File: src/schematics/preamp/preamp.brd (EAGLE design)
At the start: 50.8 x 35.6 mm, 33 parts

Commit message: Added input protection resistor to preamp
Ah input resistor was added to preamp inputs, so that short circuits of
clamping diodes won't hurt the connected device outputs.

Andrea Zoppi
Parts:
- added R17, R18: 1k, rcl:0204/5
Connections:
- new net N$3: C3.-, D3.A, D4.C, R18.2, R2.2
- new net N$8: C2.-, D1.A, D2.C, R17.2, R4.2
- net INA: now also R17.1; no longer C2.-, D1.A, D2.C, R4.2
- net INB: now also R18.1; no longer C3.-, D3.A, D4.C, R2.2
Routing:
- net N$3: track 0.00 -> 7.96 mm
- net INB: track 7.96 -> 0.00 mm
- net N$8: track 0.00 -> 7.96 mm
- net INA: track 7.96 -> 0.00 mm
- net VA: track 37.3 -> 36.2 mm
- net VB: track 36.9 -> 36.2 mm
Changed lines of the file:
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@@
 <text x="50.8" y="33.655" size="1.778" layer="51" rot="R90">G</text>
 <text x="50.8" y="31.75" size="1.778" layer="51" rot="R90">P</text>
-<text x="11.43" y="13.97" size="1.778" layer="48" rot="R90">TODO</text>
+<text x="12.7" y="10.16" size="1.778" layer="48" rot="R90">TODO</text>
 </plain>
 <attributes>
@@
 </element>
 <element name="D1" library="diode_local" package="DO35-5" value="1N4148" x="34.925" y="35.2425" smashed="yes" rot="R270">
-<attribute name="NAME" x="33.3375" y="28.829" size="1.27" layer="25" ratio="10" rot="R90"/>
+<attribute name="NAME" x="33.3375" y="27.559" size="1.27" layer="25" ratio="10" rot="R90"/>
 </element>
 <element name="D2" library="diode_local" package="DO35-5" value="1N4148" x="37.465" y="36.83" smashed="yes" rot="R90">
-<attribute name="NAME" x="34.925" y="28.829" size="1.27" layer="25" ratio="10" rot="R90"/>
+<attribute name="NAME" x="34.925" y="27.559" size="1.27" layer="25" ratio="10" rot="R90"/>
 </element>
 <element name="D3" library="diode_local" package="DO35-5" value="1N4148" x="34.925" y="10.4775" smashed="yes" rot="R90">
-<attribute name="NAME" x="33.655" y="14.5415" size="1.27" layer="25" ratio="10" rot="R90"/>
+<attribute name="NAME" x="33.655" y="16.129" size="1.27" layer="25" ratio="10" rot="R90"/>
 </element>
 <element name="D4" library="diode_local" package="DO35-5" value="1N4148" x="37.465" y="8.89" smashed="yes" rot="R270">
-<attribute name="NAME" x="35.2425" y="14.5415" size="1.27" layer="25" ratio="10" rot="R90"/>
+<attribute name="NAME" x="35.2425" y="16.129" size="1.27" layer="25" ratio="10" rot="R90"/>
 </element>
 <element name="D5" library="diode_local" package="DO35-5" value="1N4148" x="11.43" y="33.02" smashed="yes" rot="R270">
@@
 <element name="C1" library="rcl" package="E2-4" value="1u5" x="48.26" y="7.62" smashed="yes" rot="R270">
 <attribute name="NAME" x="49.149" y="9.779" size="1.27" layer="25" ratio="10"/>
+</element>
+<element name="R17" library="rcl" package="0204/5" value="1k" x="12.7" y="22.86" smashed="yes">
+<attribute name="NAME" x="11.3284" y="22.4409" size="0.9906" layer="25" ratio="10"/>
+</element>
+<element name="R18" library="rcl" package="0204/5" value="1k" x="12.7" y="20.32" smashed="yes">
+<attribute name="NAME" x="11.3284" y="19.9009" size="0.9906" layer="25" ratio="10"/>
 </element>
 </elements>
@@
 </signal>
 <signal name="INA">
-<contactref element="R4" pad="2"/>
-<contactref element="D1" pad="A"/>
-<contactref element="D2" pad="C"/>
-<contactref element="C2" pad="-"/>
-<wire x1="39.6875" y1="31.75" x2="39.6875" y2="34.29" width="0.6096" layer="16"/>
-<wire x1="39.6875" y1="34.29" x2="37.465" y2="34.29" width="0.6096" layer="16"/>
-<wire x1="34.925" y1="32.7025" x2="35.8775" y2="32.7025" width="0.6096" layer="16"/>
-<wire x1="35.8775" y1="32.7025" x2="37.465" y2="34.29" width="0.6096" layer="16"/>
+<contactref element="R17" pad="1"/>
 </signal>
 <signal name="BIAS">
@@
 <contactref element="U1" pad="3"/>
 <contactref element="U1" pad="12"/>
-<wire x1="22.225" y1="16.51" x2="22.225" y2="20.32" width="0.6096" layer="16"/>
-<wire x1="22.225" y1="20.32" x2="23.495" y2="21.59" width="0.6096" layer="16"/>
-<wire x1="23.495" y1="21.59" x2="33.02" y2="21.59" width="0.6096" layer="16"/>
+<wire x1="22.225" y1="16.51" x2="22.225" y2="20.6375" width="0.6096" layer="16"/>
+<wire x1="22.225" y1="20.6375" x2="23.1775" y2="21.59" width="0.6096" layer="16"/>
+<wire x1="23.1775" y1="21.59" x2="33.02" y2="21.59" width="0.6096" layer="16"/>
 <wire x1="33.02" y1="21.59" x2="34.29" y2="20.32" width="0.6096" layer="16"/>
 <wire x1="34.29" y1="20.32" x2="34.29" y2="19.05" width="0.6096" layer="16"/>
@@
 </signal>
 <signal name="INB">
-<contactref element="R2" pad="2"/>
-<contactref element="D3" pad="A"/>
-<contactref element="D4" pad="C"/>
-<contactref element="C3" pad="-"/>
-<wire x1="39.6875" y1="13.97" x2="39.6875" y2="11.43" width="0.6096" layer="16"/>
-<wire x1="39.6875" y1="11.43" x2="37.465" y2="11.43" width="0.6096" layer="16"/>
-<wire x1="34.925" y1="13.0175" x2="35.8775" y2="13.0175" width="0.6096" layer="16"/>
-<wire x1="35.8775" y1="13.0175" x2="37.465" y2="11.43" width="0.6096" layer="16"/>
+<contactref element="R18" pad="1"/>
 </signal>
 <signal name="N$9">
@@
 <wire x1="39.37" y1="26.67" x2="39.37" y2="25.4" width="0.6096" layer="16"/>
 <wire x1="39.37" y1="25.4" x2="38.1" y2="24.13" width="0.6096" layer="16"/>
-<wire x1="38.1" y1="24.13" x2="36.83" y2="24.13" width="0.6096" layer="16"/>
-<via x="36.83" y="24.13" extent="1-16" drill="0.6" shape="square"/>
-<wire x1="36.83" y1="24.13" x2="21.59" y2="24.13" width="0.6096" layer="1"/>
-<via x="21.59" y="24.13" extent="1-16" drill="0.6" diameter="1.27" shape="octagon"/>
-<wire x1="21.59" y1="24.13" x2="21.59" y2="26.035" width="0.6096" layer="16"/>
+<via x="38.1" y="24.13" extent="1-16" drill="0.6" diameter="1.27" shape="octagon"/>
+<wire x1="38.1" y1="24.13" x2="23.495" y2="24.13" width="0.6096" layer="1"/>
+<wire x1="23.495" y1="24.13" x2="21.59" y2="26.035" width="0.6096" layer="1"/>
+<via x="21.59" y="26.035" extent="1-16" drill="0.6" diameter="1.27" shape="octagon"/>
 <wire x1="21.59" y1="26.035" x2="18.415" y2="29.21" width="0.6096" layer="16"/>
 <wire x1="18.415" y1="29.21" x2="17.78" y2="29.21" width="0.6096" layer="16"/>
@@
 <wire x1="39.37" y1="19.05" x2="39.37" y2="20.32" width="0.6096" layer="16"/>
 <wire x1="39.37" y1="20.32" x2="38.1" y2="21.59" width="0.6096" layer="16"/>
-<wire x1="38.1" y1="21.59" x2="36.83" y2="21.59" width="0.6096" layer="16"/>
-<via x="36.83" y="21.59" extent="1-16" drill="0.6" diameter="1.27" shape="octagon"/>
-<wire x1="36.83" y1="21.59" x2="21.59" y2="21.59" width="0.6096" layer="1"/>
-<wire x1="21.59" y1="21.59" x2="19.05" y2="24.13" width="0.6096" layer="1"/>
-<via x="19.05" y="24.13" extent="1-16" drill="0.6" diameter="1.27" shape="octagon"/>
-<wire x1="19.05" y1="24.13" x2="19.05" y2="25.4" width="0.6096" layer="16"/>
-<wire x1="19.05" y1="25.4" x2="17.78" y2="26.67" width="0.6096" layer="16"/>
+<via x="38.1" y="21.59" extent="1-16" drill="0.6" diameter="1.27" shape="octagon"/>
+<wire x1="38.1" y1="21.59" x2="22.86" y2="21.59" width="0.6096" layer="1"/>
+<wire x1="22.86" y1="21.59" x2="20.32" y2="24.13" width="0.6096" layer="1"/>
+<via x="20.32" y="24.13" extent="1-16" drill="0.6" diameter="1.27" shape="octagon"/>
+<wire x1="20.32" y1="24.13" x2="17.78" y2="26.67" width="0.6096" layer="16"/>
 </signal>
 <signal name="N$6">
@@
 <contactref element="R14" pad="1"/>
 <contactref element="U1" pad="7"/>
-<wire x1="24.13" y1="26.67" x2="24.13" y2="24.13" width="0.6096" layer="16"/>
-<wire x1="24.13" y1="24.13" x2="19.685" y2="19.685" width="0.6096" layer="16"/>
-<wire x1="19.685" y1="19.685" x2="19.685" y2="17.78" width="0.6096" layer="16"/>
+<wire x1="24.13" y1="26.67" x2="24.13" y2="24.765" width="0.6096" layer="16"/>
+<wire x1="24.13" y1="24.765" x2="19.685" y2="20.32" width="0.6096" layer="16"/>
+<wire x1="19.685" y1="20.32" x2="19.685" y2="17.78" width="0.6096" layer="16"/>
+</signal>
+<signal name="N$2">
+</signal>
+<signal name="N$3">
+<contactref element="R18" pad="2"/>
+<contactref element="C3" pad="-"/>
+<contactref element="D3" pad="A"/>
+<contactref element="D4" pad="C"/>
+<contactref element="R2" pad="2"/>
+<wire x1="39.6875" y1="13.97" x2="39.6875" y2="11.43" width="0.6096" layer="16"/>
+<wire x1="39.6875" y1="11.43" x2="37.465" y2="11.43" width="0.6096" layer="16"/>
+<wire x1="37.465" y1="11.43" x2="36.5125" y2="11.43" width="0.6096" layer="16"/>
+<wire x1="36.5125" y1="11.43" x2="34.925" y2="13.0175" width="0.6096" layer="16"/>
+<wire x1="15.24" y1="20.32" x2="34.925" y2="13.0175" width="0" layer="19" extent="1-1"/>
+</signal>
+<signal name="N$8">
+<contactref element="R17" pad="2"/>
+<contactref element="C2" pad="-"/>
+<contactref element="D1" pad="A"/>
+<contactref element="D2" pad="C"/>
+<contactref element="R4" pad="2"/>
+<wire x1="39.6875" y1="31.75" x2="39.6875" y2="34.29" width="0.6096" layer="16"/>
+<wire x1="39.6875" y1="34.29" x2="37.465" y2="34.29" width="0.6096" layer="16"/>
+<wire x1="37.465" y1="34.29" x2="36.5125" y2="34.29" width="0.6096" layer="16"/>
+<wire x1="36.5125" y1="34.29" x2="34.925" y2="32.7025" width="0.6096" layer="16"/>
+<wire x1="15.24" y1="22.86" x2="34.925" y2="32.7025" width="0" layer="19" extent="1-1"/>
 </signal>
 </signals>

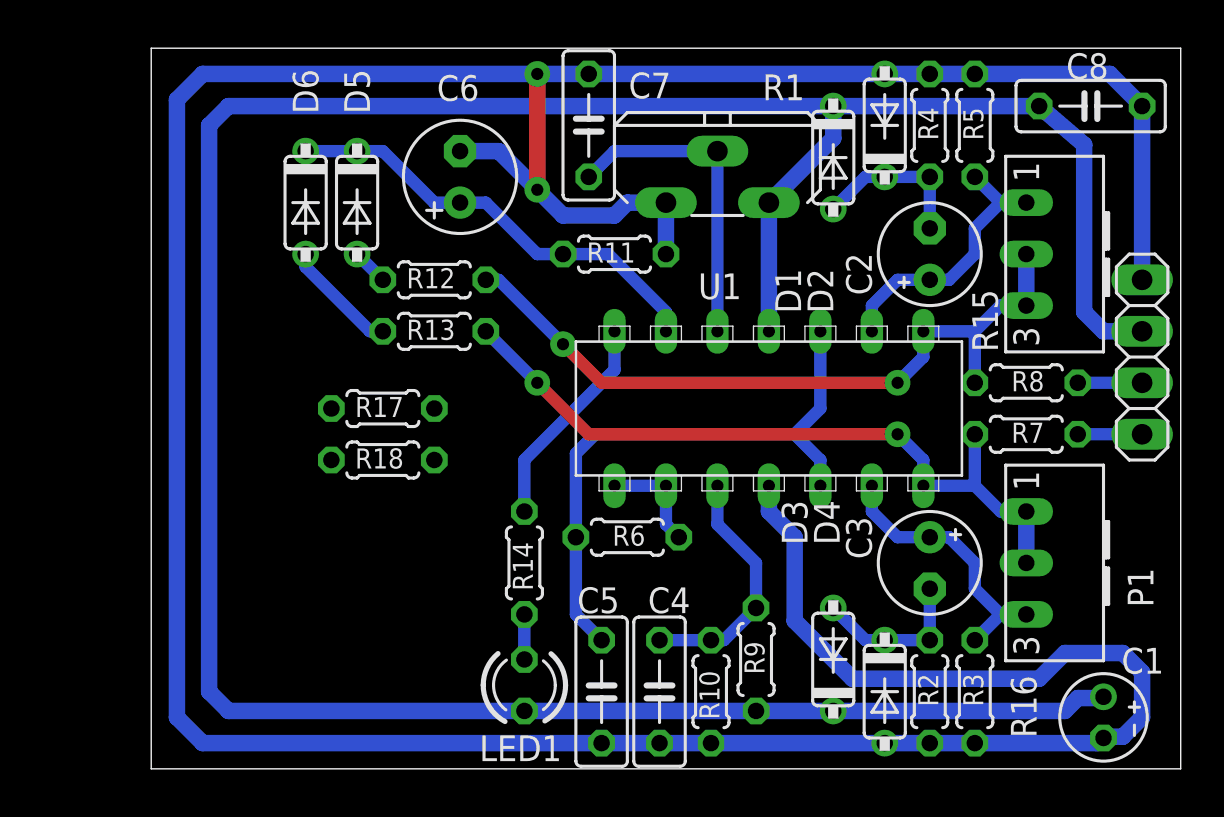
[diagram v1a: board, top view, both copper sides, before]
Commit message: Added double RCA connector to preamp module
Andrea Zoppi
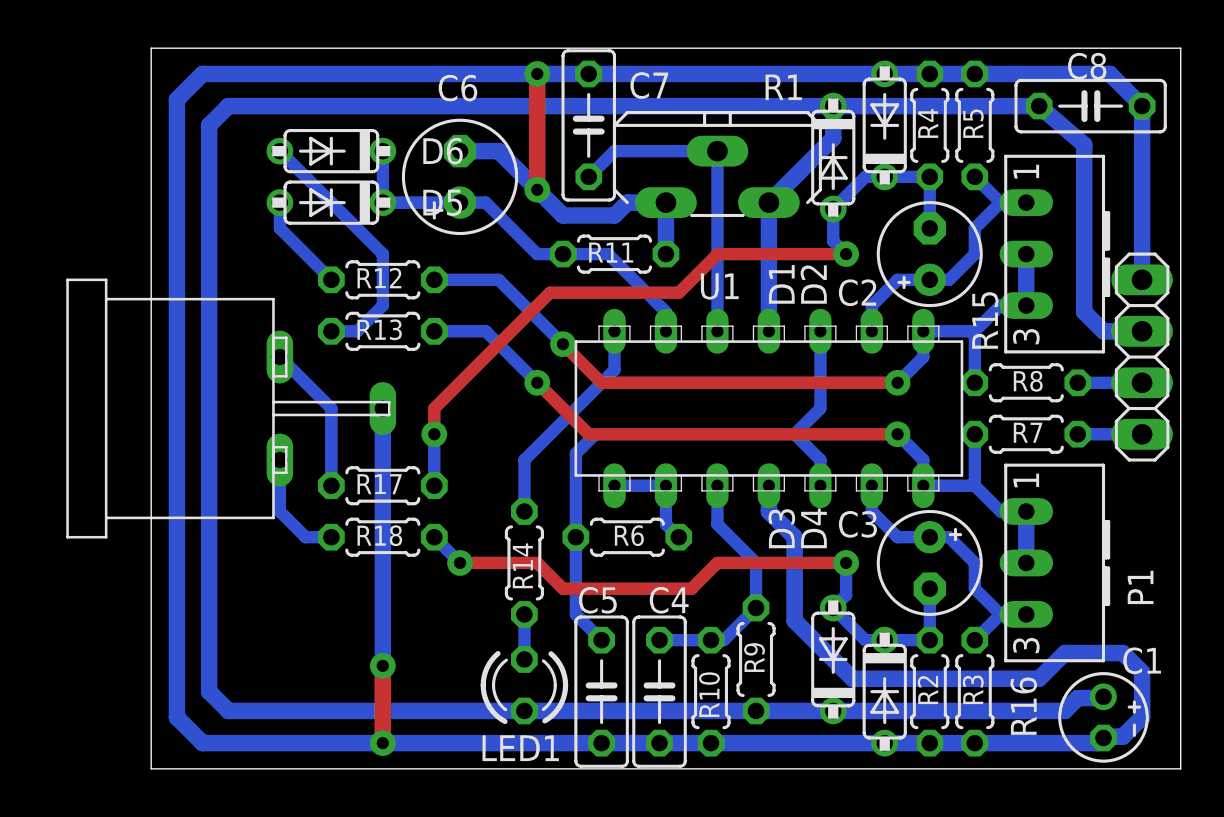
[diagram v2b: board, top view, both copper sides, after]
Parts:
- added RCA1: RCA-2V, con_local:RCA-2V
- moved R17 3.81 mm to (12.7, 19.1)
- moved R18 3.81 mm to (12.7, 16.5)
- moved D6 2.84 mm to (10.2, 35.6), turned to 180 degrees
- moved R12 2.54 mm to (12.7, 29.2)
- moved R13 2.54 mm to (12.7, 26.7)
- moved D5 1.27 mm to (10.2, 33.0), turned to 180 degrees
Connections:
- net GND: now also RCA1.SHIELD
- net INA: now also RCA1.L
- net INB: now also RCA1.R
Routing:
- net N$8: track 7.96 -> 37.7 mm, vias 0 -> 2
- net N$3: track 7.96 -> 32.3 mm, vias 0 -> 2
- net GND: track 185.2 -> 201.7 mm, vias 2 -> 4
- net INA: track 0.00 -> 7.40 mm
- net N$11: track 5.76 -> 12.8 mm
- net INB: track 0.00 -> 5.61 mm
- net N$10: track 1.80 -> 4.86 mm
- net VB: track 36.2 -> 38.7 mm
- net VA: track 36.2 -> 38.7 mm
- net N$4: track 22.0 -> 19.7 mm
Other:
- board text removed: "TODO"

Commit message: Trimmable preamp positive reference
The preamp positive voltage reference is now trimmable, so that it can be
calibrated in order to reduce misalignments with the main board's internal
reference (internal DAC output of the PIC).

Preamp board schematics refactored.

Andrea Zoppi
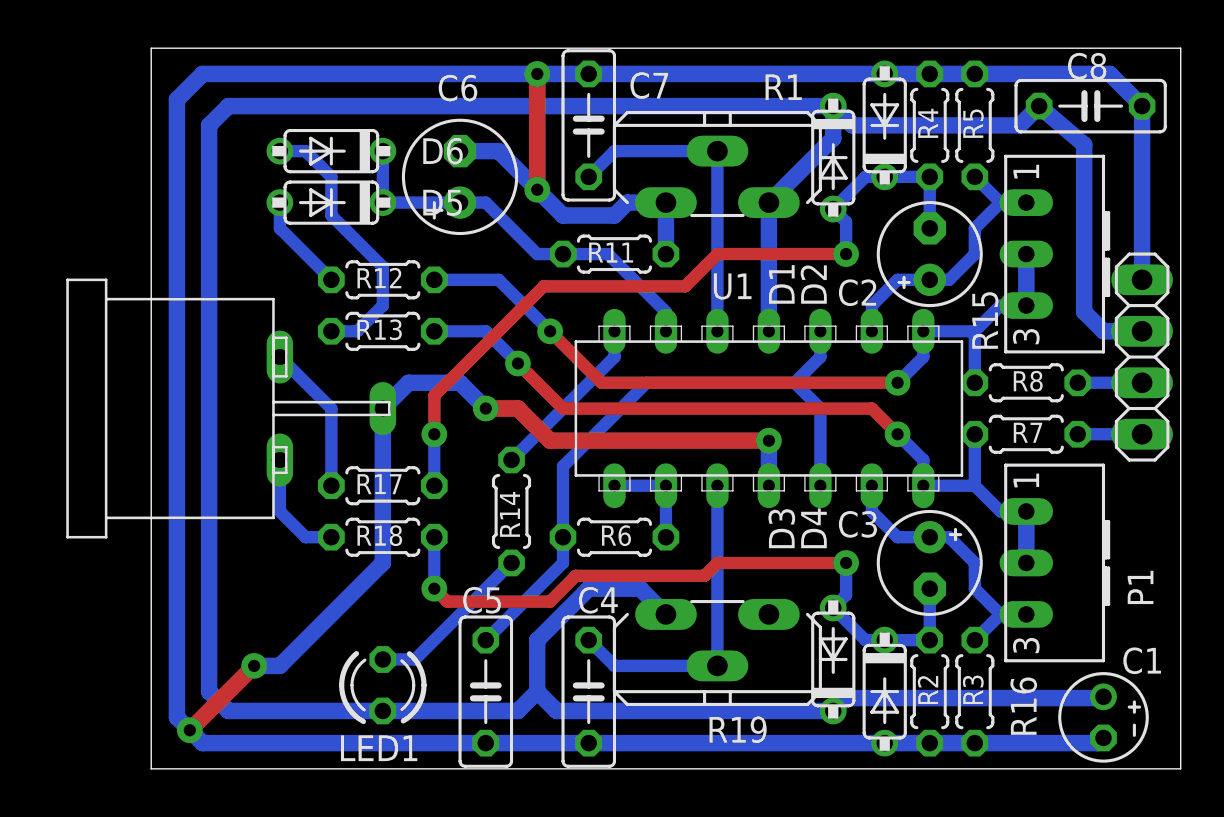
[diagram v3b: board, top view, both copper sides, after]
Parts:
- removed R10, R9: 10k, rcl:0204/5
- added R19: 47k, pot:PT-10S
- moved LED1 6.98 mm to (12.7, 9.21)
- moved C5 5.71 mm to (17.8, 8.89)
- moved C4 3.49 mm to (22.9, 8.89)
- moved R14 2.62 mm to (19.1, 17.8)
- moved R6 0.64 mm to (24.1, 16.5)
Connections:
- new net N$14: R19.A
- net +3V3: now also R19.E; no longer R9.2
- net GND: no longer R10.1
- net N$1: now also R19.S; no longer R10.2, R9.1
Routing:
- net +3V3: track 140.9 -> 153.0 mm
- net N$12: track 2.22 -> 8.32 mm
- net GND: track 201.7 -> 197.8 mm, vias 4 -> 6
- net N$1: track 12.2 -> 15.8 mm
- net BIAS: track 29.6 -> 32.0 mm
- net N$13: track 10.7 -> 8.45 mm
- net N$3: track 32.3 -> 34.4 mm
- net N$11: track 12.8 -> 13.5 mm

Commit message: Window comparator for preamp calibration
The positive voltage reference for opamps is now reduced to a simple
potentiometer, sithout impedance decoupling (not strictly needed).

Two opamps are used as comparators for windowing of the rectified input
signals. This way it is possible to warn the user if the signal is too low
like before (bad comparator results) and also if the signal is too strong,
thus leading to a potentially wring duty cycle of the squared wave.

Andrea Zoppi
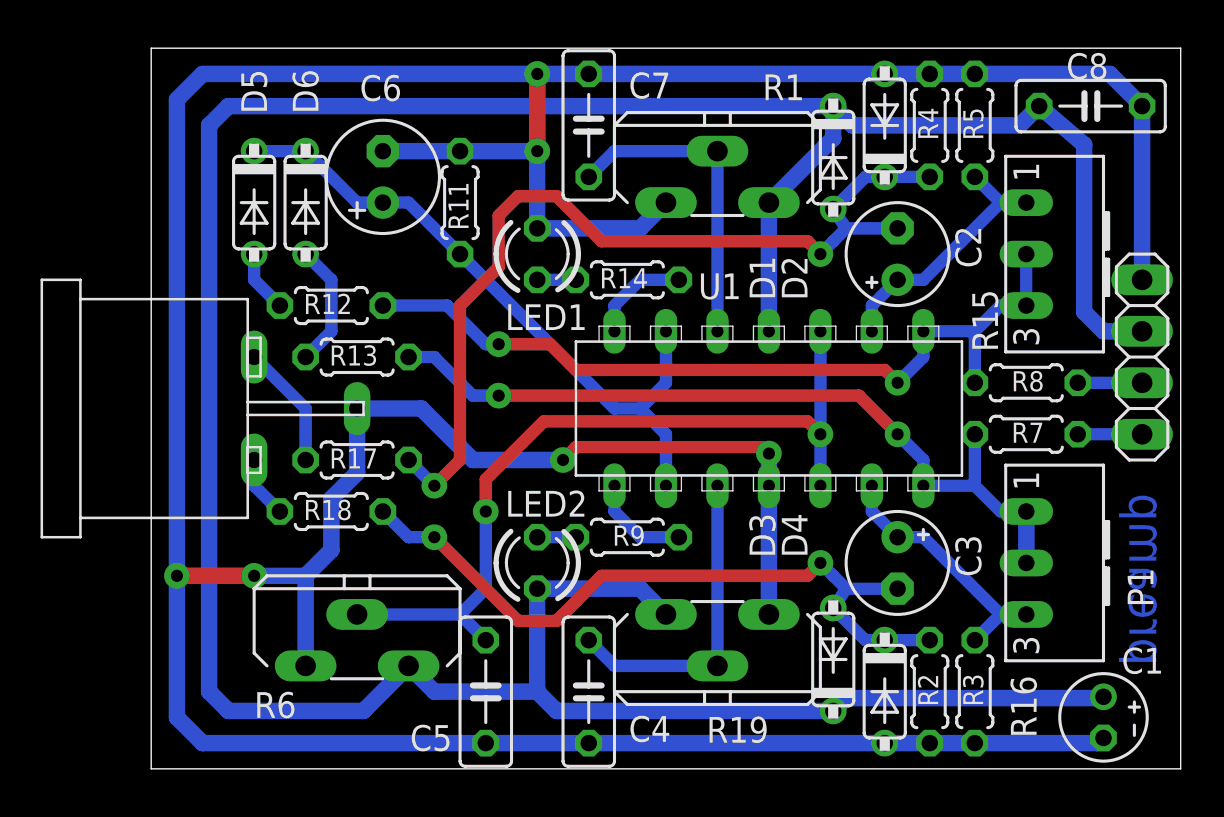
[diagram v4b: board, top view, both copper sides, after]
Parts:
- added LED2: red, led:LED3MM
- added R9: 470, rcl:0204/5
- R6: value 1k -> 47k; device rcl:0204/5 -> pot:PT-10S
- moved LED1 22.6 mm to (20.3, 30.5)
- moved R6 13.7 mm to (11.4, 11.4), turned to 0 degrees
- moved R14 12.8 mm to (24.8, 29.2), turned to 180 degrees
- moved R11 8.03 mm to (16.5, 33.0), turned to 270 degrees
- moved C6 3.81 mm to (12.7, 34.3)
- moved D5 3.81 mm to (6.35, 33.0), turned to 270 degrees
- moved D6 2.84 mm to (8.89, 33.0), turned to 270 degrees
- moved R12 2.84 mm to (10.2, 27.9)
- moved R18 2.84 mm to (10.2, 17.8)
- moved R13 1.80 mm to (11.4, 25.4)
- moved R17 1.80 mm to (11.4, 20.3)
- moved C2 1.59 mm to (38.1, 30.5)
- moved C3 1.59 mm to (38.1, 15.2)
- moved RCA1 1.27 mm to (8.89, 22.9)
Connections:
- net INA renamed INL
- net INB renamed INR
- net OUTA renamed OUTL
- net OUTB renamed OUTR
- net VA renamed VL
- net VB renamed VR
- removed net N$14: R19.A
- new net N$2: R9.1, U1.8
- net +3V3: now also LED2.A, R6.E; no longer LED1.A
- net BIAS: now also R6.S; no longer R6.2
- net GND: now also LED1.K, R19.A, R6.A
- net N$12: now also LED2.K, R9.2; no longer LED1.K, R14.2
- net N$4: now also U1.9
- net N$7: now also LED1.A, R14.2; no longer R6.1, U1.8, U1.9
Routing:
- net N$4: track 19.7 -> 33.0 mm
- net GND: track 197.8 -> 206.2 mm
- net BIAS: track 32.0 -> 39.6 mm, vias 0 -> 2
- net N$11: track 13.5 -> 6.13 mm
- net N$8: track 38.1 -> 44.8 mm
- net N$12: track 8.32 -> 1.91 mm
- net N$2: track 0.00 -> 4.97 mm
- net N$13: track 8.45 -> 4.97 mm
- net N$7: track 5.08 -> 1.91 mm
- net +3V3: track 153.0 -> 155.5 mm
- net INR: track 5.61 -> 3.07 mm
- net VL: track 38.7 -> 40.7 mm
- net N$10: track 4.86 -> 3.07 mm
- net N$3: track 34.4 -> 35.9 mm
- net INL: track 7.40 -> 6.13 mm
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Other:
- board text added: "preamp"
